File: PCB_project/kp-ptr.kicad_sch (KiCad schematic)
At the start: 38 parts, among them J1 ESP32_PROG_CON, U1 ESP32-C3FH4, Y2 XRCGB40M000F4M00R0

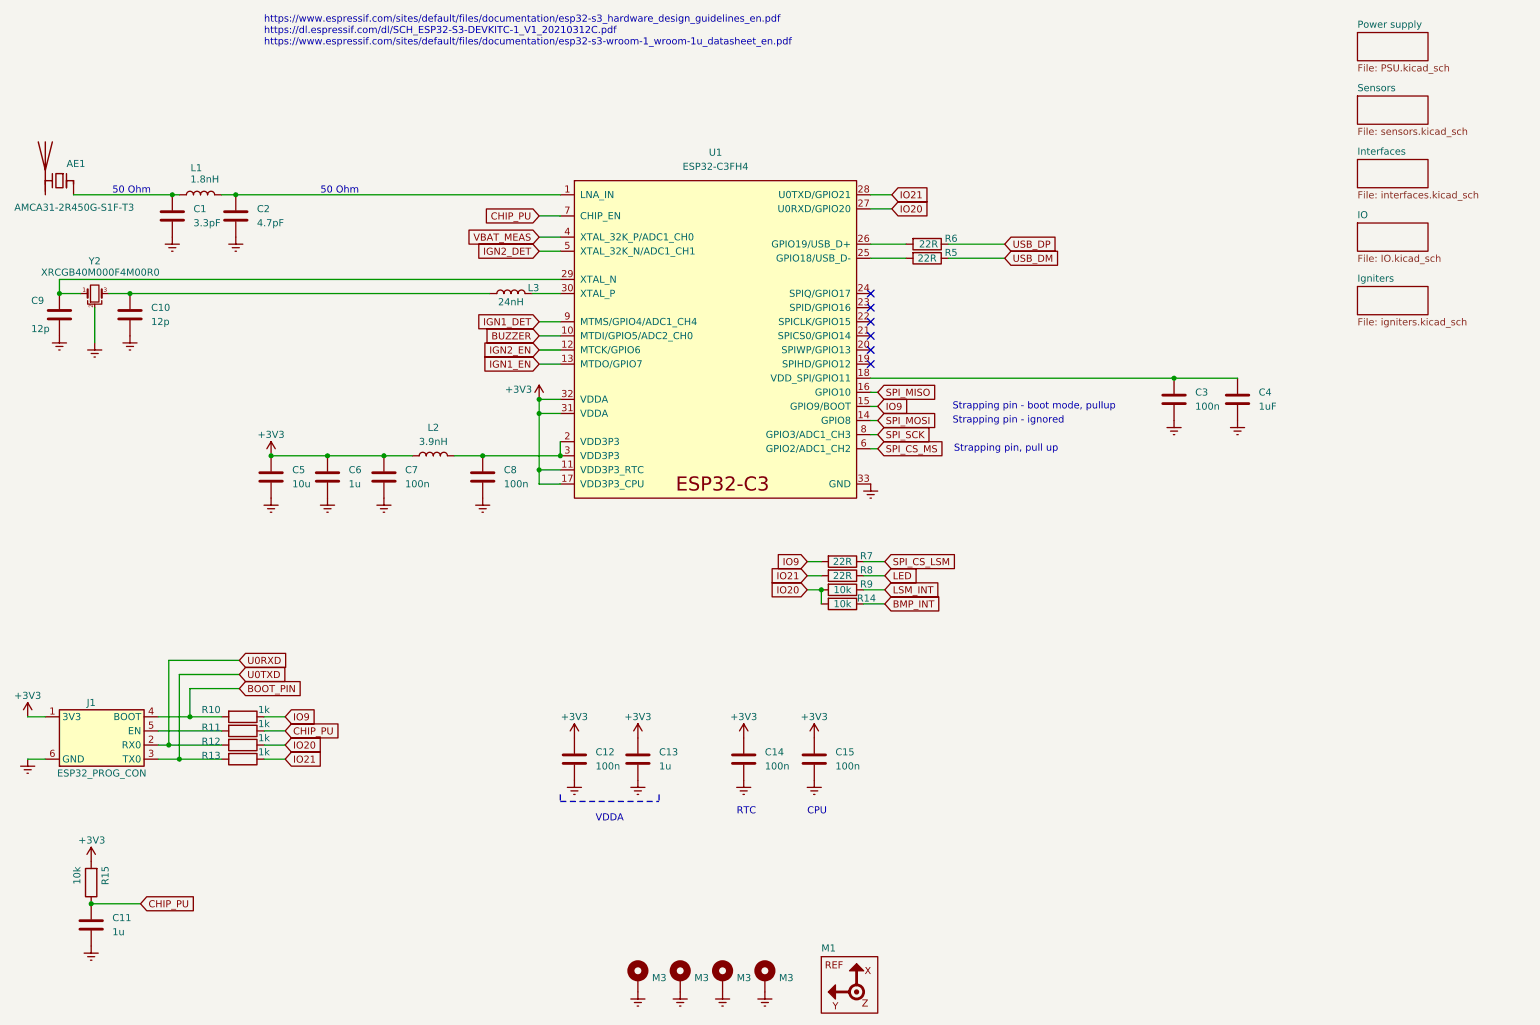
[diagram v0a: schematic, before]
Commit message: Almost ready version. Require more GND vias etc
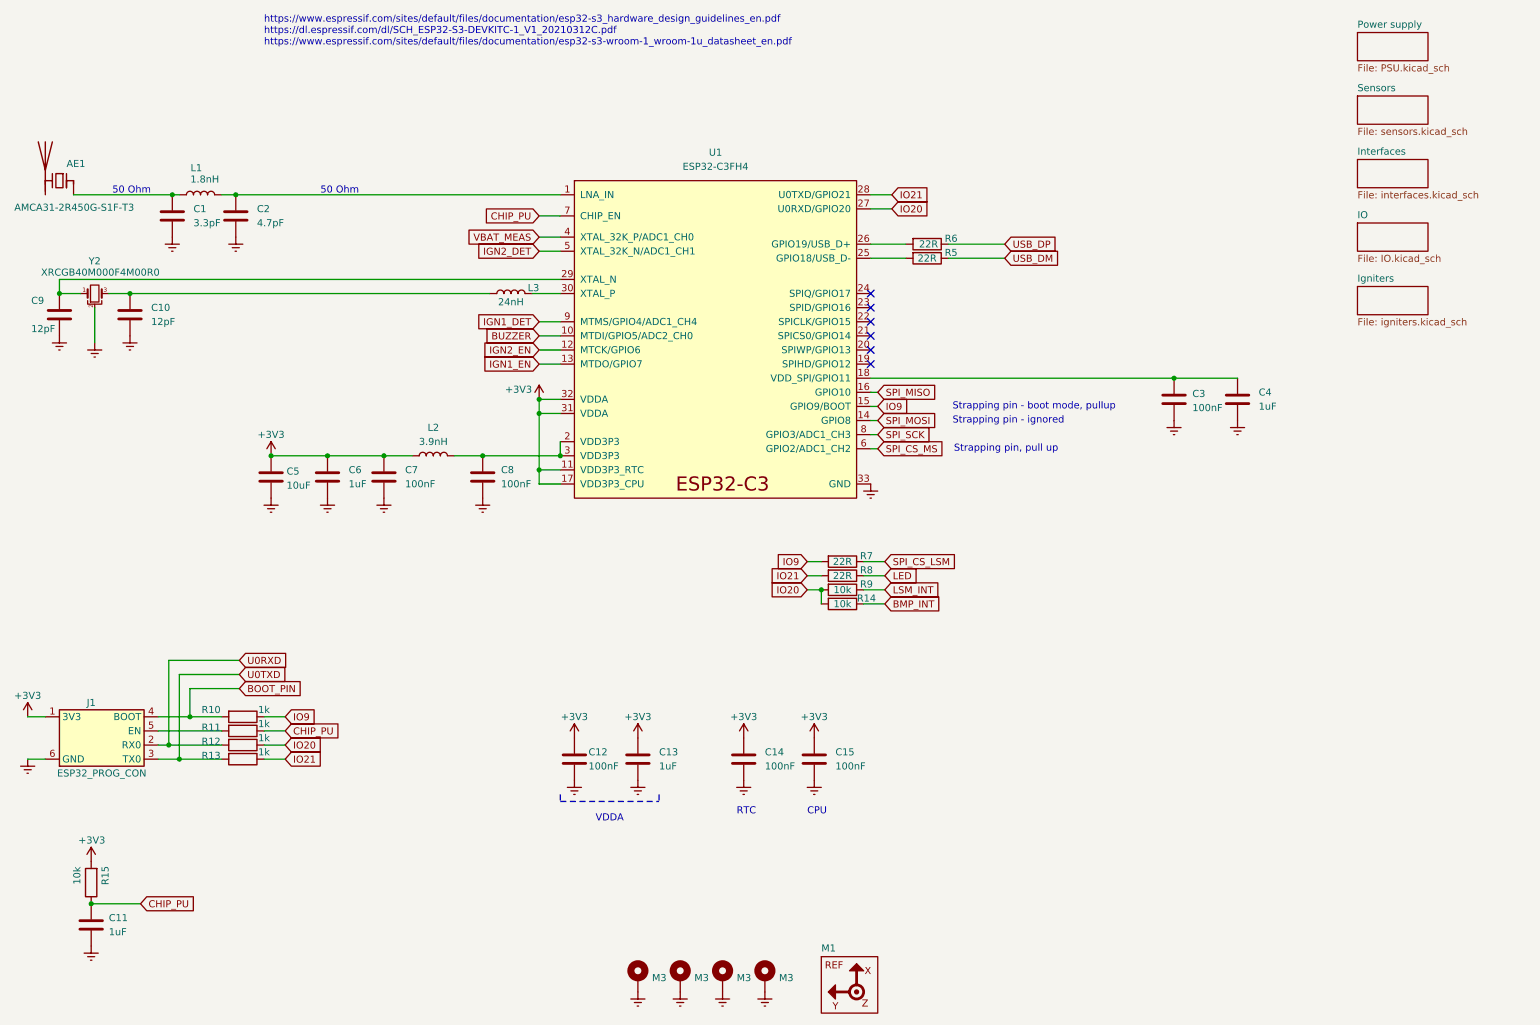
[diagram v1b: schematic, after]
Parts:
- C10, C9: value 12p -> 12pF
- C11, C13, C6: value 1u -> 1uF
- C12, C14, C15, C3, C7, C8: value 100n -> 100nF
- C5: value 10u -> 10uF; footprint Capacitor_SMD:C_0402_1005Metric -> Capacitor_SMD:C_0603_1608Metric
- J1, M1: now left out of the parts list
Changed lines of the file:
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@@
 		(in_bom no)
 		(on_board yes)
-		(in_pos_files yes)
+		(in_pos_files no)
 		(dnp no)
 		(fields_autoplaced yes)
@@
 		(in_pos_files yes)
 		(dnp no)
-		(fields_autoplaced yes)
 		(property "Reference" "C3"
-			(at 228.6 83.8199 0)
+			(at 228.092 84.074 0)
 			(show_name no)
 			(do_not_autoplace no)
@@
 			)
 		)
-		(property "Value" "100n"
-			(at 228.6 86.3599 0)
+		(property "Value" "100nF"
+			(at 228.092 86.614 0)
 			(show_name no)
 			(do_not_autoplace no)
@@
 			)
 		)
-		(property "Value" "12p"
+		(property "Value" "12pF"
 			(at 40.64 71.1199 0)
 			(show_name no)
@@
 		(in_bom no)
 		(on_board yes)
-		(in_pos_files yes)
+		(in_pos_files no)
 		(dnp no)
 		(fields_autoplaced yes)
@@
 		(in_bom no)
 		(on_board yes)
-		(in_pos_files yes)
+		(in_pos_files no)
 		(dnp no)
 		(fields_autoplaced yes)
@@
 			)
 		)
-		(property "Value" "100n"
+		(property "Value" "100nF"
 			(at 86.36 100.3299 0)
 			(show_name no)
@@
 		(in_bom no)
 		(on_board yes)
-		(in_pos_files yes)
+		(in_pos_files no)
 		(dnp no)
 		(fields_autoplaced yes)
@@
 		(in_pos_files yes)
 		(dnp no)
-		(fields_autoplaced yes)
 		(property "Reference" "C5"
-			(at 66.04 97.7899 0)
+			(at 65.024 98.044 0)
 			(show_name no)
 			(do_not_autoplace no)
@@
 			)
 		)
-		(property "Value" "10u"
-			(at 66.04 100.3299 0)
+		(property "Value" "10uF"
+			(at 65.024 100.584 0)
 			(show_name no)
 			(do_not_autoplace no)
@@
 			)
 		)
-		(property "Footprint" "Capacitor_SMD:C_0402_1005Metric"
+		(property "Footprint" "Capacitor_SMD:C_0603_1608Metric"
 			(at 63.1952 102.87 0)
 			(hide yes)
@@
 		(in_pos_files yes)
 		(dnp no)
-		(fields_autoplaced yes)
 		(property "Reference" "C12"
-			(at 120.65 148.5899 0)
+			(at 119.38 148.59 0)
 			(show_name no)
 			(do_not_autoplace no)
@@
 			)
 		)
-		(property "Value" "100n"
-			(at 120.65 151.1299 0)
+		(property "Value" "100nF"
+			(at 119.38 151.13 0)
 			(show_name no)
 			(do_not_autoplace no)
@@
 			)
 		)
-		(property "Value" "1u"
+		(property "Value" "1uF"
 			(at 76.2 100.3299 0)
 			(show_name no)
@@
 			)
 		)
-		(property "Value" "100n"
+		(property "Value" "100nF"
 			(at 163.83 151.1299 0)
 			(show_name no)
@@
 		(body_style 1)
 		(exclude_from_sim no)
-		(in_bom yes)
+		(in_bom no)
 		(on_board yes)
-		(in_pos_files yes)
+		(in_pos_files no)
 		(dnp no)
 		(property "Reference" "J1"
@@
 		(in_pos_files yes)
 		(dnp no)
-		(fields_autoplaced yes)
 		(property "Reference" "C8"
-			(at 104.14 97.7899 0)
+			(at 103.632 97.79 0)
 			(show_name no)
 			(do_not_autoplace no)
@@
 			)
 		)
-		(property "Value" "100n"
-			(at 104.14 100.3299 0)
+		(property "Value" "100nF"
+			(at 103.632 100.33 0)
 			(show_name no)
 			(do_not_autoplace no)
@@
 		(fields_autoplaced yes)
 		(property "Reference" "C11"
-			(at 33.655 178.4349 0)
+			(at 33.02 178.4349 0)
 			(show_name no)
 			(do_not_autoplace no)
@@
 			)
 		)
-		(property "Value" "1u"
-			(at 33.655 180.9749 0)
+		(property "Value" "1uF"
+			(at 33.02 180.9749 0)
 			(show_name no)
 			(do_not_autoplace no)
@@
 			)
 		)
-		(property "Value" "12p"
+		(property "Value" "12pF"
 			(at 19.05 72.39 0)
 			(show_name no)
@@
 		(body_style 1)
 		(exclude_from_sim no)
-		(in_bom yes)
+		(in_bom no)
 		(on_board yes)
-		(in_pos_files yes)
+		(in_pos_files no)
 		(dnp no)
 		(property "Reference" "M1"
@@
 			)
 		)
-		(property "Value" "1u"
+		(property "Value" "1uF"
 			(at 132.08 151.1299 0)
 			(show_name no)
@@
 			)
 		)
-		(property "Value" "100n"
+		(property "Value" "100nF"
 			(at 151.13 151.1299 0)
 			(show_name no)
